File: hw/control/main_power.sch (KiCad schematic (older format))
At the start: 9 parts

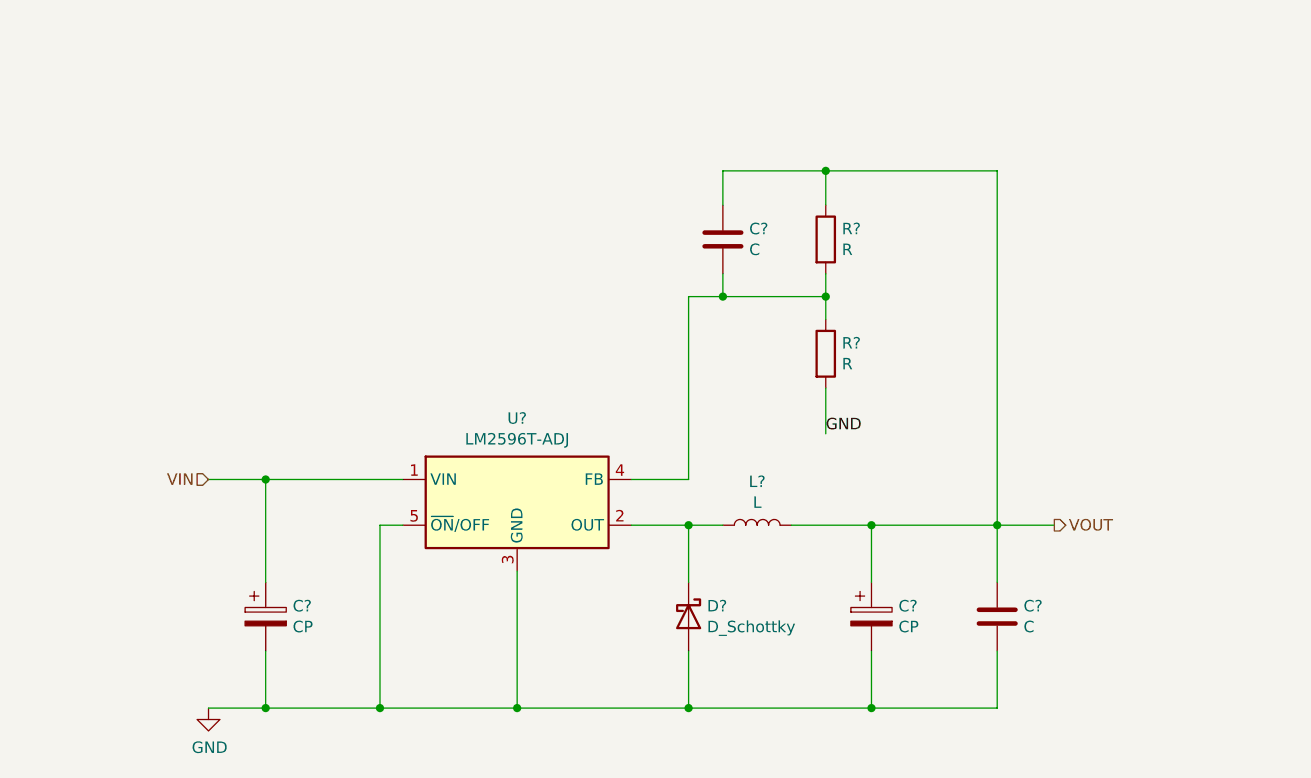
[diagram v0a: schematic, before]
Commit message: [hw] Add LED bus driver
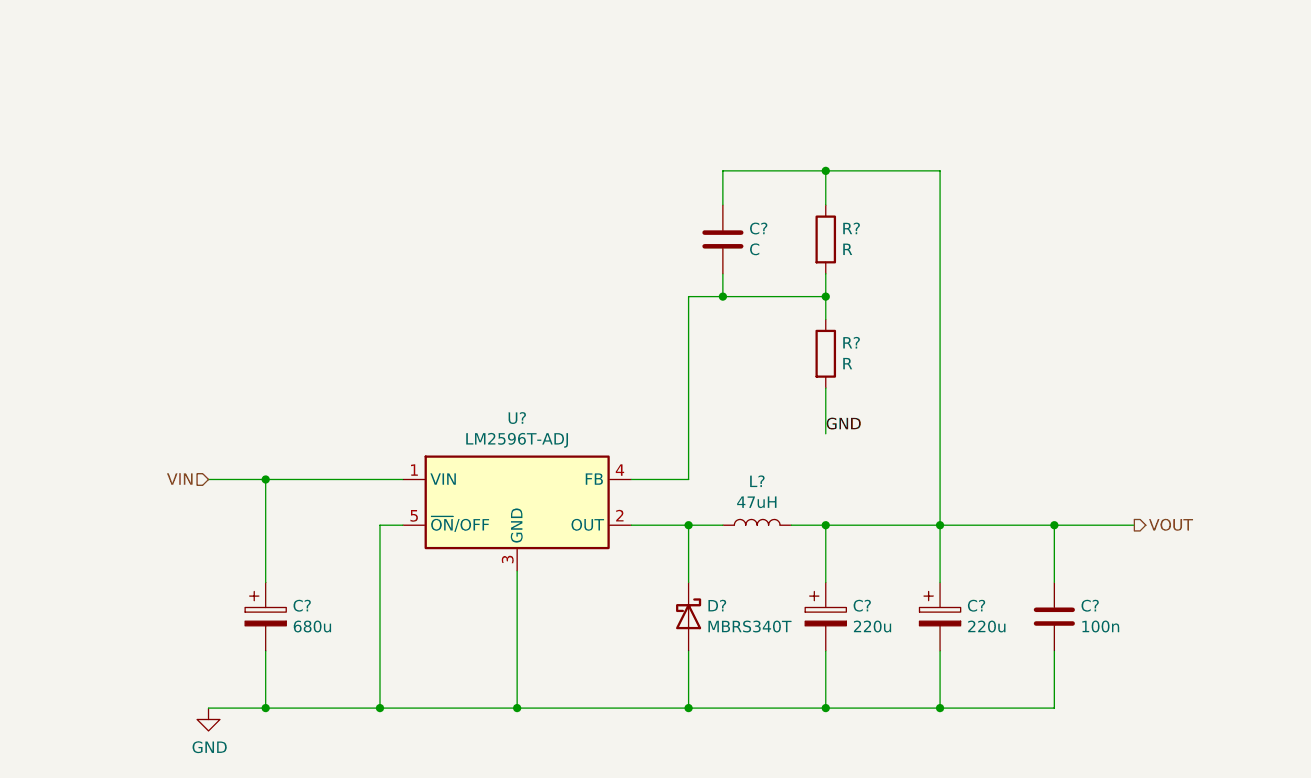
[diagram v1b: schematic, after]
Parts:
- added C?: 220u, symbol Device:CP
- C?: value CP -> 220u
- C?: value CP -> 680u
- C?: value C -> 100n
- D?: value D_Schottky -> MBRS340T
- L?: value L -> 47uH
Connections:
- net GND: now also C?.2
- net VOUT: now also C?.1
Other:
- moved on the sheet: C?
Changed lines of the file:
@@
 Text HLabel 4300 3500 0    50   Input ~ 0
 VIN
-Text HLabel 8000 3700 2    50   Output ~ 0
+Text HLabel 8350 3700 2    50   Output ~ 0
 VOUT
 $Comp
@@
 P 6400 4100
 F 0 "D?" V 6354 4180 50  0000 L CNN
-F 1 "D_Schottky" V 6445 4180 50  0000 L CNN
+F 1 "MBRS340T" V 6445 4180 50  0000 L CNN
 F 2 "" H 6400 4100 50  0001 C CNN
 F 3 "~" H 6400 4100 50  0001 C CNN
@@
 P 6700 3700
 F 0 "L?" V 6890 3700 50  0000 C CNN
-F 1 "L" V 6799 3700 50  0000 C CNN
+F 1 "47uH" V 6799 3700 50  0000 C CNN
 F 2 "" H 6700 3700 50  0001 C CNN
 F 3 "~" H 6700 3700 50  0001 C CNN
@@
 L Device:CP C?
 U 1 1 6147DC54
-P 7200 4100
-F 0 "C?" H 7318 4146 50  0000 L CNN
-F 1 "CP" H 7318 4055 50  0000 L CNN
-F 2 "" H 7238 3950 50  0001 C CNN
-F 3 "~" H 7200 4100 50  0001 C CNN
-	1    7200 4100
+P 7500 4100
+F 0 "C?" H 7618 4146 50  0000 L CNN
+F 1 "220u" H 7618 4055 50  0000 L CNN
+F 2 "" H 7538 3950 50  0001 C CNN
+F 3 "~" H 7500 4100 50  0001 C CNN
+	1    7500 4100
 	1    0    0    -1
 $EndComp
@@
 P 4550 4100
 F 0 "C?" H 4668 4146 50  0000 L CNN
-F 1 "CP" H 4668 4055 50  0000 L CNN
+F 1 "680u" H 4668 4055 50  0000 L CNN
 F 2 "" H 4588 3950 50  0001 C CNN
 F 3 "~" H 4550 4100 50  0001 C CNN
@@
 Wire Wire Line
 	4550 3500 5150 3500
-Wire Wire Line
-	6850 3700 7200 3700
-Wire Wire Line
-	7200 3950 7200 3700
-Connection ~ 7200 3700
-Wire Wire Line
-	7200 4250 7200 4500
-Wire Wire Line
-	7200 4500 6400 4500
-Connection ~ 6400 4500
 $Comp
 L Device:C C?
 U 1 1 61480AF3
-P 7750 4100
-F 0 "C?" H 7865 4146 50  0000 L CNN
-F 1 "C" H 7865 4055 50  0000 L CNN
-F 2 "" H 7788 3950 50  0001 C CNN
-F 3 "~" H 7750 4100 50  0001 C CNN
-	1    7750 4100
-	1    0    0    -1
-$EndComp
-Wire Wire Line
-	7200 4500 7750 4500
-Wire Wire Line
-	7750 4500 7750 4250
-Connection ~ 7200 4500
-Wire Wire Line
-	7200 3700 7750 3700
-Wire Wire Line
-	7750 3950 7750 3700
-Connection ~ 7750 3700
-Wire Wire Line
-	7750 3700 8000 3700
+P 8000 4100
+F 0 "C?" H 8115 4146 50  0000 L CNN
+F 1 "100n" H 8115 4055 50  0000 L CNN
+F 2 "" H 8038 3950 50  0001 C CNN
+F 3 "~" H 8000 4100 50  0001 C CNN
+	1    8000 4100
+	1    0    0    -1
+$EndComp
 $Comp
 L Device:R R?
@@
 	7000 2300 7000 2150
 Wire Wire Line
-	7000 2150 7750 2150
-Wire Wire Line
-	7750 2150 7750 3700
-Wire Wire Line
 	7000 2700 6550 2700
 Wire Wire Line
@@
 Wire Wire Line
 	6550 2150 7000 2150
-Connection ~ 7000 2150
 Wire Wire Line
 	4300 3500 4550 3500
@@
 	1    0    0    -1
 $EndComp
+$Comp
+L Device:CP C?
+U 1 1 6145F282
+P 7000 4100
+F 0 "C?" H 7118 4146 50  0000 L CNN
+F 1 "220u" H 7118 4055 50  0000 L CNN
+F 2 "" H 7038 3950 50  0001 C CNN
+F 3 "~" H 7000 4100 50  0001 C CNN
+	1    7000 4100
+	1    0    0    -1
+$EndComp
+Wire Wire Line
+	6400 4500 7000 4500
+Wire Wire Line
+	7000 4500 7000 4250
+Connection ~ 6400 4500
+Wire Wire Line
+	7000 4500 7500 4500
+Wire Wire Line
+	7500 4500 7500 4250
+Connection ~ 7000 4500
+Wire Wire Line
+	7500 4500 8000 4500
+Wire Wire Line
+	8000 4500 8000 4250
+Connection ~ 7500 4500
+Wire Wire Line
+	6850 3700 7000 3700
+Wire Wire Line
+	7000 3700 7000 3950
+Wire Wire Line
+	7000 3700 7500 3700
+Wire Wire Line
+	7500 3700 7500 3950
+Connection ~ 7000 3700
+Wire Wire Line
+	7500 3700 8000 3700
+Wire Wire Line
+	8000 3700 8000 3950
+Connection ~ 7500 3700
+Wire Wire Line
+	8000 3700 8350 3700
+Connection ~ 8000 3700
+Wire Wire Line
+	7000 2150 7500 2150
+Wire Wire Line
+	7500 2150 7500 3700
+Connection ~ 7000 2150
 $EndSCHEMATC

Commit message: [hw] Add annotations, minor fixes
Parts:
- D201: renamed from D?; value MBRS340T -> ???
- gave numbers to parts that had none: 9
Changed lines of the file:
@@
 encoding utf-8
 Sheet 2 7
-Title ""
-Date ""
-Rev ""
-Comp ""
-Comment1 ""
+Title "WS2812 Controller"
+Date "2021-09-16"
+Rev "1"
+Comp "Stefan Misik"
+Comment1 "Main Power Supply"
 Comment2 ""
 Comment3 ""
@@
 VOUT
 $Comp
-L Regulator_Switching:LM2596T-ADJ U?
+L Regulator_Switching:LM2596T-ADJ U201
 U 1 1 6147458B
 P 5650 3600
-F 0 "U?" H 5650 3967 50  0000 C CNN
+F 0 "U201" H 5650 3967 50  0000 C CNN
 F 1 "LM2596T-ADJ" H 5650 3876 50  0000 C CNN
 F 2 "Package_TO_SOT_THT:TO-220-5_P3.4x3.7mm_StaggerOdd_Lead3.8mm_Vertical" H 5700 3350 50  0001 L CIN
@@
 	6400 3950 6400 3700
 $Comp
-L Device:D_Schottky D?
+L Device:D_Schottky D201
 U 1 1 61479AF5
 P 6400 4100
-F 0 "D?" V 6354 4180 50  0000 L CNN
-F 1 "MBRS340T" V 6445 4180 50  0000 L CNN
+F 0 "D201" V 6354 4180 50  0000 L CNN
+F 1 "???" V 6445 4180 50  0000 L CNN
 F 2 "" H 6400 4100 50  0001 C CNN
 F 3 "~" H 6400 4100 50  0001 C CNN
@@
 	6400 4250 6400 4500
 $Comp
-L Device:L L?
+L Device:L L201
 U 1 1 6147CE04
 P 6700 3700
-F 0 "L?" V 6890 3700 50  0000 C CNN
+F 0 "L201" V 6890 3700 50  0000 C CNN
 F 1 "47uH" V 6799 3700 50  0000 C CNN
 F 2 "" H 6700 3700 50  0001 C CNN
@@
 Connection ~ 6400 3700
 $Comp
-L Device:CP C?
+L Device:CP C204
 U 1 1 6147DC54
 P 7500 4100
-F 0 "C?" H 7618 4146 50  0000 L CNN
+F 0 "C204" H 7618 4146 50  0000 L CNN
 F 1 "220u" H 7618 4055 50  0000 L CNN
 F 2 "" H 7538 3950 50  0001 C CNN
@@
 $EndComp
 $Comp
-L Device:CP C?
+L Device:CP C202
 U 1 1 6147E42F
 P 4550 4100
-F 0 "C?" H 4668 4146 50  0000 L CNN
+F 0 "C202" H 4668 4146 50  0000 L CNN
 F 1 "680u" H 4668 4055 50  0000 L CNN
 F 2 "" H 4588 3950 50  0001 C CNN
@@
 	4550 3500 5150 3500
 $Comp
-L Device:C C?
+L Device:C C205
 U 1 1 61480AF3
 P 8000 4100
-F 0 "C?" H 8115 4146 50  0000 L CNN
+F 0 "C205" H 8115 4146 50  0000 L CNN
 F 1 "100n" H 8115 4055 50  0000 L CNN
 F 2 "" H 8038 3950 50  0001 C CNN
@@
 $EndComp
 $Comp
-L Device:R R?
+L Device:R R202
 U 1 1 61481E1C
 P 7000 2950
-F 0 "R?" H 7070 2996 50  0000 L CNN
+F 0 "R202" H 7070 2996 50  0000 L CNN
 F 1 "R" H 7070 2905 50  0000 L CNN
 F 2 "" V 6930 2950 50  0001 C CNN
@@
 $EndComp
 $Comp
-L Device:R R?
+L Device:R R201
 U 1 1 614831F3
 P 7000 2450
-F 0 "R?" H 7070 2496 50  0000 L CNN
+F 0 "R201" H 7070 2496 50  0000 L CNN
 F 1 "R" H 7070 2405 50  0000 L CNN
 F 2 "" V 6930 2450 50  0001 C CNN
@@
 Wire Wire Line
 	7000 2600 7000 2700
-Text Label 7000 3300 0    50   ~ 0
-GND
-Wire Wire Line
-	7000 3300 7000 3100
+Wire Wire Line
+	7000 3200 7000 3100
 Wire Wire Line
 	7000 2300 7000 2150
@@
 	7000 2700 7000 2800
 $Comp
-L Device:C C?
+L Device:C C201
 U 1 1 61484750
 P 6550 2450
-F 0 "C?" H 6665 2496 50  0000 L CNN
+F 0 "C201" H 6665 2496 50  0000 L CNN
 F 1 "C" H 6665 2405 50  0000 L CNN
 F 2 "" H 6588 2300 50  0001 C CNN
@@
 Connection ~ 4550 3500
 $Comp
-L power:GND #PWR0104
+L power:GND #PWR0202
 U 1 1 614AABF3
 P 4300 4500
-F 0 "#PWR0104" H 4300 4250 50  0001 C CNN
+F 0 "#PWR0202" H 4300 4250 50  0001 C CNN
 F 1 "GND" H 4305 4327 50  0000 C CNN
 F 2 "" H 4300 4500 50  0001 C CNN
@@
 $EndComp
 $Comp
-L Device:CP C?
+L Device:CP C203
 U 1 1 6145F282
 P 7000 4100
-F 0 "C?" H 7118 4146 50  0000 L CNN
+F 0 "C203" H 7118 4146 50  0000 L CNN
 F 1 "220u" H 7118 4055 50  0000 L CNN
 F 2 "" H 7038 3950 50  0001 C CNN
@@
 	7500 2150 7500 3700
 Connection ~ 7000 2150
+$Comp
+L power:GND #PWR0201
+U 1 1 61493959
+P 7000 3200
+F 0 "#PWR0201" H 7000 2950 50  0001 C CNN
+F 1 "GND" H 7005 3027 50  0000 C CNN
+F 2 "" H 7000 3200 50  0001 C CNN
+F 3 "" H 7000 3200 50  0001 C CNN
+	1    7000 3200
+	1    0    0    -1
+$EndComp
 $EndSCHEMATC

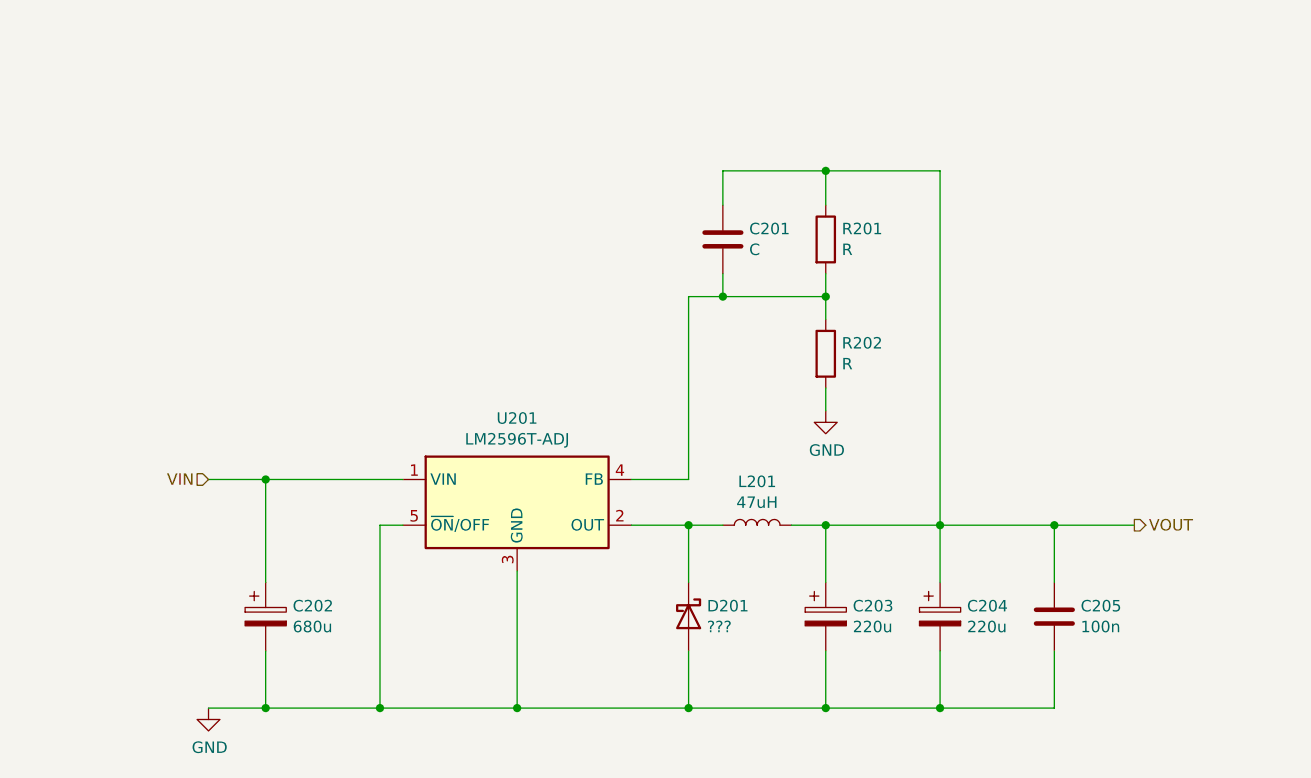
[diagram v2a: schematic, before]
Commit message: [hw] Add LED driver output sheets
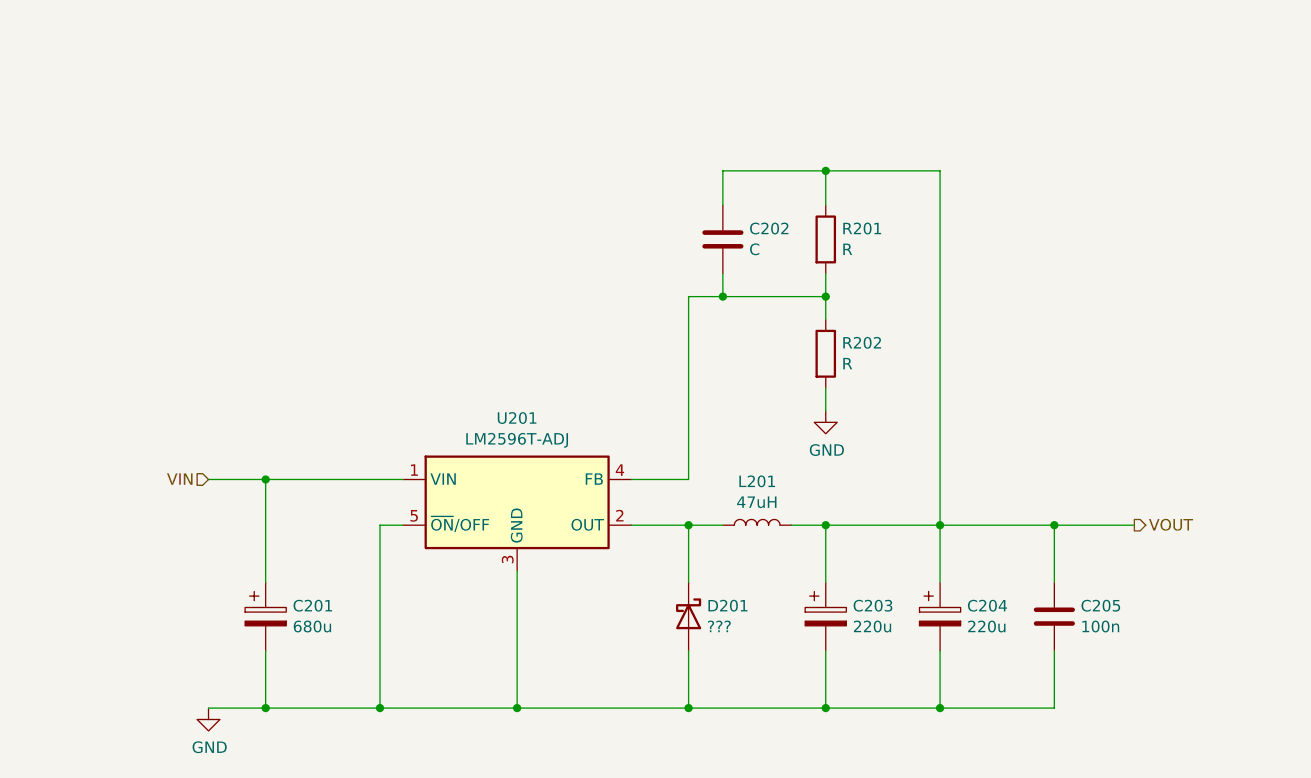
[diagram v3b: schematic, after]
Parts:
- renumbered C202 to C201, C201 to C202
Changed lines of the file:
@@
 $Descr A4 11693 8268
 encoding utf-8
-Sheet 2 7
+Sheet 2 9
 Title "WS2812 Controller"
-Date "2021-09-16"
+Date "2021-09-21"
 Rev "1"
 Comp "Stefan Misik"
@@
 $EndComp
 $Comp
-L Device:CP C202
+L Device:CP C201
 U 1 1 6147E42F
 P 4550 4100
-F 0 "C202" H 4668 4146 50  0000 L CNN
+F 0 "C201" H 4668 4146 50  0000 L CNN
 F 1 "680u" H 4668 4055 50  0000 L CNN
 F 2 "" H 4588 3950 50  0001 C CNN
@@
 	7000 2700 7000 2800
 $Comp
-L Device:C C201
+L Device:C C202
 U 1 1 61484750
 P 6550 2450
-F 0 "C201" H 6665 2496 50  0000 L CNN
+F 0 "C202" H 6665 2496 50  0000 L CNN
 F 1 "C" H 6665 2405 50  0000 L CNN
 F 2 "" H 6588 2300 50  0001 C CNN
@@
 Connection ~ 4550 3500
 $Comp
-L power:GND #PWR0202
+L power:GND #PWR0201
 U 1 1 614AABF3
 P 4300 4500
-F 0 "#PWR0202" H 4300 4250 50  0001 C CNN
+F 0 "#PWR0201" H 4300 4250 50  0001 C CNN
 F 1 "GND" H 4305 4327 50  0000 C CNN
 F 2 "" H 4300 4500 50  0001 C CNN
@@
 Connection ~ 7000 2150
 $Comp
-L power:GND #PWR0201
+L power:GND #PWR0202
 U 1 1 61493959
 P 7000 3200
-F 0 "#PWR0201" H 7000 2950 50  0001 C CNN
+F 0 "#PWR0202" H 7000 2950 50  0001 C CNN
 F 1 "GND" H 7005 3027 50  0000 C CNN
 F 2 "" H 7000 3200 50  0001 C CNN

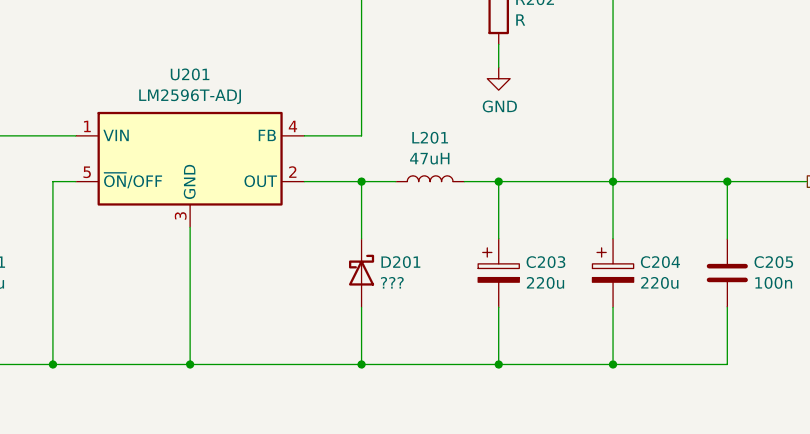
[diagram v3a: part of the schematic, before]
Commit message: [hw] Add some component types
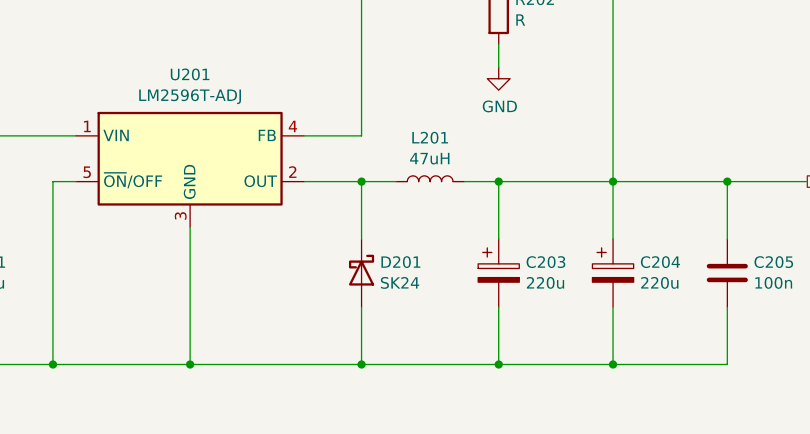
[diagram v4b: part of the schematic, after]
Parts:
- D201: value ??? -> SK24
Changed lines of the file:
@@
 P 6400 4100
 F 0 "D201" V 6354 4180 50  0000 L CNN
-F 1 "???" V 6445 4180 50  0000 L CNN
+F 1 "SK24" V 6445 4180 50  0000 L CNN
 F 2 "" H 6400 4100 50  0001 C CNN
 F 3 "~" H 6400 4100 50  0001 C CNN
